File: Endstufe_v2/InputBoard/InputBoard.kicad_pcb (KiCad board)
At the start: 4 copper layers, 57 parts, among them J1 ST-0322D00-071-1A2H, J11 DNP, J2 ST-0322D00-071-1A2H, J3 ST-0322D00-071-1A2H, J4 ST-0322D00-071-1A2H, J5 B4B-XH-2_(LF)(SN), J6 B4B-XH-2_(LF)(SN), J7 B4B-XH-2_(LF)(SN), J8 Conn_01x02_Pin, J9 B4B-XH-2_(LF)(SN), U1 PCM1865DBTR, U2 PCM9211PTR, U4 ZPLR135_T8, U5 ZPLR135_T8, U6 ZPLR135_T8, U7 ZPLR135_T8, Y1 24.576Mhz, Y2 24.576Mhz

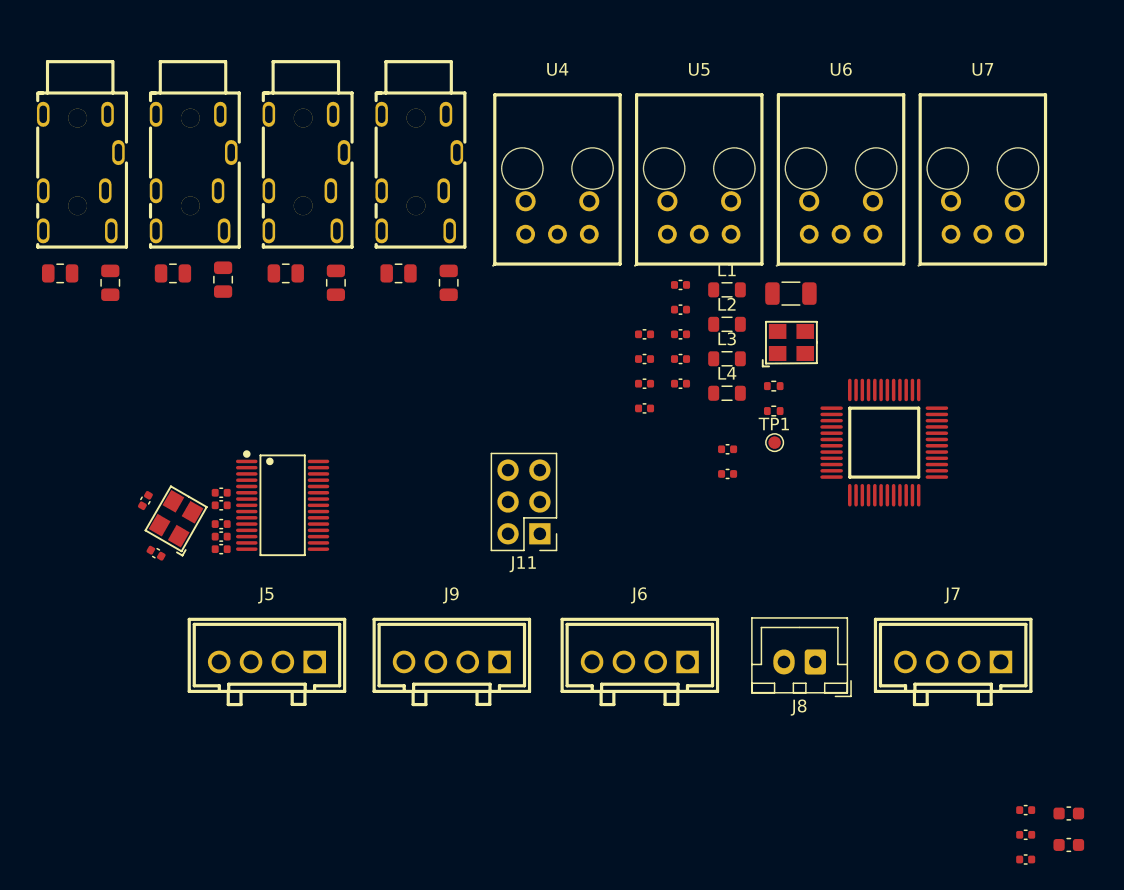
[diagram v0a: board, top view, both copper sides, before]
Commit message: Continue working on input board and use ADAU1467 instaed of ADAU1463
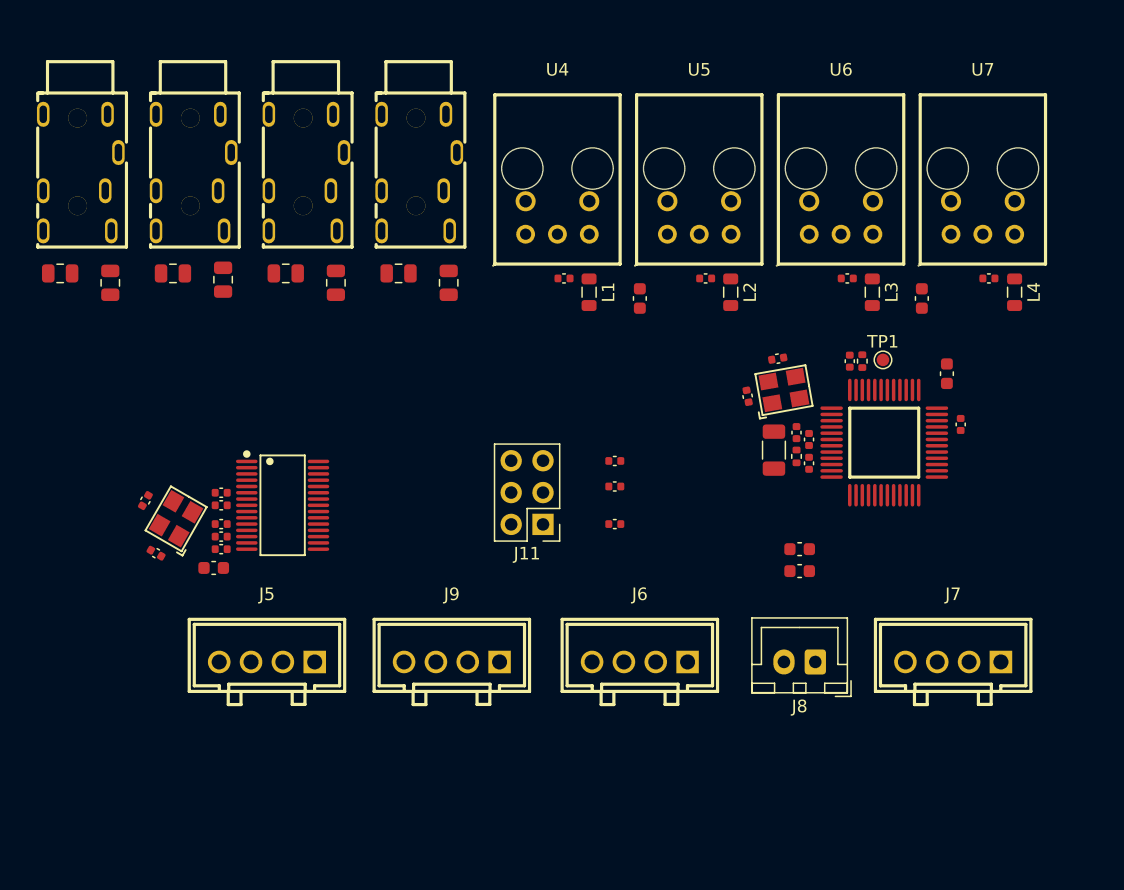
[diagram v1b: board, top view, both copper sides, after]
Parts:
- added C30: 22uF, Endstufe:C_0603_1608Metric, F.Cu at (119.0, 88.0)
- added C31: 22uF, Endstufe:C_0603_1608Metric, F.Cu at (141.5, 88.0)
- added C32: 22uF, Endstufe:C_0603_1608Metric, F.Cu at (85.0, 109.5)
- added C33: 22uF, Endstufe:C_0603_1608Metric, F.Cu at (143.5, 94.0)
- moved R2 43.0 mm to (117.0, 101.0)
- moved R3 43.0 mm to (117.0, 103.0)
- moved R5 42.3 mm to (117.0, 106.0)
- moved C29 30.6 mm to (131.8, 109.8)
- moved C28 30.1 mm to (131.8, 108.0)
- moved C15 25.8 mm to (144.6, 98.0), turned to 90 degrees
- moved C18 24.6 mm to (146.8, 86.4)
- moved L4 24.3 mm to (148.9, 87.5), turned to -90 degrees
- moved C14 16.5 mm to (135.8, 93.0), turned to -90 degrees
- moved C24 15.7 mm to (135.6, 86.4)
- moved C20 14.6 mm to (132.5, 99.2), turned to 90 degrees
- moved C17 13.8 mm to (132.5, 101.2), turned to -90 degrees
- moved L3 12.8 mm to (137.6, 87.5), turned to -90 degrees
- moved C16 12.7 mm to (131.5, 98.7), turned to -90 degrees
- moved C21 12.6 mm to (129.7, 100.1), turned to -90 degrees
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
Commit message: Continue layouting
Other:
- board outline added: 85 x 50 mm
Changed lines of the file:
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@@
 		(tags "capacitor")
 		(property "Reference" "C29"
-			(at 0 -1.43 360)
+			(at 0 -1.43 0)
 			(layer "F.SilkS")
 			(hide yes)
@@
 		)
 		(property "Value" "22uF"
-			(at 0 1.43 360)
+			(at 0 1.43 0)
 			(layer "F.Fab")
 			(effects
@@
 		)
 		(property "Footprint" "Endstufe:C_0603_1608Metric"
-			(at 0 0 360)
+			(at 0 0 0)
 			(layer "F.Fab")
 			(hide yes)
@@
 		)
 		(property "Datasheet" ""
-			(at 0 0 360)
+			(at 0 0 0)
 			(layer "F.Fab")
 			(hide yes)
@@
 		)
 		(property "Description" ""
-			(at 0 0 360)
+			(at 0 0 0)
 			(layer "F.Fab")
 			(hide yes)
@@
 		)
 		(property "LCSC Part #" "C59461"
-			(at 0 0 360)
+			(at 0 0 0)
 			(layer "F.Fab")
 			(hide yes)
@@
 		)
 		(fp_text user "${REFERENCE}"
-			(at 0 0 360)
+			(at 0 0 0)
 			(layer "F.Fab")
 			(effects
@@
 			(end -5 3.694996)
 			(stroke
-				(width 0.254001)
+				(width 0.254)
 				(type solid)
 			)
@@
 			(end 5 -9.805029)
 			(stroke
-				(width 0.254001)
+				(width 0.254)
 				(type solid)
 			)
@@
 			(end 5 3.694996)
 			(stroke
-				(width 0.254001)
+				(width 0.254)
 				(type solid)
 			)
@@
 			(end 5 3.694996)
 			(stroke
-				(width 0.254001)
+				(width 0.254)
 				(type solid)
 			)
@@
 		(tags "capacitor")
 		(property "Reference" "C32"
-			(at 0 -1.43 360)
+			(at 0 -1.43 0)
 			(layer "F.SilkS")
 			(hide yes)
@@
 		)
 		(property "Value" "22uF"
-			(at 0 1.43 360)
+			(at 0 1.43 0)
 			(layer "F.Fab")
 			(effects
@@
 		)
 		(property "Footprint" "Endstufe:C_0603_1608Metric"
-			(at 0 0 360)
+			(at 0 0 0)
 			(layer "F.Fab")
 			(hide yes)
@@
 		)
 		(property "Datasheet" ""
-			(at 0 0 360)
+			(at 0 0 0)
 			(layer "F.Fab")
 			(hide yes)
@@
 		)
 		(property "Description" ""
-			(at 0 0 360)
+			(at 0 0 0)
 			(layer "F.Fab")
 			(hide yes)
@@
 		)
 		(property "LCSC Part #" "C59461"
-			(at 0 0 360)
+			(at 0 0 0)
 			(layer "F.Fab")
 			(hide yes)
@@
 		)
 		(fp_text user "${REFERENCE}"
-			(at 0 0 360)
+			(at 0 0 0)
 			(layer "F.Fab")
 			(effects
@@
 		(tags "capacitor")
 		(property "Reference" "C28"
-			(at 0 -1.43 360)
+			(at 0 -1.43 0)
 			(layer "F.SilkS")
 			(hide yes)
@@
 		)
 		(property "Value" "22uF"
-			(at 0 1.43 360)
+			(at 0 1.43 0)
 			(layer "F.Fab")
 			(effects
@@
 		)
 		(property "Footprint" "Endstufe:C_0603_1608Metric"
-			(at 0 0 360)
+			(at 0 0 0)
 			(layer "F.Fab")
 			(hide yes)
@@
 		)
 		(property "Datasheet" ""
-			(at 0 0 360)
+			(at 0 0 0)
 			(layer "F.Fab")
 			(hide yes)
@@
 		)
 		(property "Description" ""
-			(at 0 0 360)
+			(at 0 0 0)
 			(layer "F.Fab")
 			(hide yes)
@@
 		)
 		(property "LCSC Part #" "C59461"
-			(at 0 0 360)
+			(at 0 0 0)
 			(layer "F.Fab")
 			(hide yes)
@@
 		)
 		(fp_text user "${REFERENCE}"
-			(at 0 0 360)
+			(at 0 0 0)
 			(layer "F.Fab")
 			(effects
@@
 			(end -5 3.694996)
 			(stroke
-				(width 0.254001)
+				(width 0.254)
 				(type solid)
 			)
@@
 			(end 5 -9.805029)
 			(stroke
-				(width 0.254001)
+				(width 0.254)
 				(type solid)
 			)
@@
 			(end 5 3.694996)
 			(stroke
-				(width 0.254001)
+				(width 0.254)
 				(type solid)
 			)
@@
 			(end 5 3.694996)
 			(stroke
-				(width 0.254001)
+				(width 0.254)
 				(type solid)
 			)
@@
 			(end -5 3.694996)
 			(stroke
-				(width 0.254001)
+				(width 0.254)
 				(type solid)
 			)
@@
 			(end 5 -9.805029)
 			(stroke
-				(width 0.254001)
+				(width 0.254)
 				(type solid)
 			)
@@
 			(end 5 3.694996)
 			(stroke
-				(width 0.254001)
+				(width 0.254)
 				(type solid)
 			)
@@
 			(end 5 3.694996)
 			(stroke
-				(width 0.254001)
+				(width 0.254)
 				(type solid)
 			)
@@
 		(tags "capacitor")
 		(property "Reference" "C18"
-			(at 0 -1.16 360)
+			(at 0 -1.16 0)
 			(layer "F.SilkS")
 			(hide yes)
@@
 		)
 		(property "Value" "100nF"
-			(at 0 1.16 360)
+			(at 0 1.16 0)
 			(layer "F.Fab")
 			(effects
@@
 		)
 		(property "Footprint" "Endstufe:C_0402_1005Metric"
-			(at 0 0 360)
+			(at 0 0 0)
 			(layer "F.Fab")
 			(hide yes)
@@
 		)
 		(property "Datasheet" ""
-			(at 0 0 360)
+			(at 0 0 0)
 			(layer "F.Fab")
 			(hide yes)
@@
 		)
 		(property "Description" ""
-			(at 0 0 360)
+			(at 0 0 0)
 			(layer "F.Fab")
 			(hide yes)
@@
 		)
 		(property "LCSC Part #" "C307331"
-			(at 0 0 360)
+			(at 0 0 0)
 			(layer "F.Fab")
 			(hide yes)
@@
 		)
 		(fp_text user "${REFERENCE}"
-			(at 0 0 360)
+			(at 0 0 0)
 			(layer "F.Fab")
 			(effects
@@
 		(tags "capacitor")
 		(property "Reference" "R2"
-			(at 0 -1.16 360)
+			(at 0 -1.16 0)
 			(layer "F.SilkS")
 			(hide yes)
@@
 		)
 		(property "Value" "10k"
-			(at 0 1.16 360)
+			(at 0 1.16 0)
 			(layer "F.Fab")
 			(effects
@@
 		)
 		(property "Footprint" "Endstufe:C_0402_1005Metric"
-			(at 0 0 360)
+			(at 0 0 0)
 			(layer "F.Fab")
 			(hide yes)
@@
 		)
 		(property "Datasheet" ""
-			(at 0 0 360)
+			(at 0 0 0)
 			(layer "F.Fab")
 			(hide yes)
@@
 		)
 		(property "Description" ""
-			(at 0 0 360)
+			(at 0 0 0)
 			(layer "F.Fab")
 			(hide yes)
@@
 		)
 		(property "LCSC Part #" "C25744"
-			(at 0 0 360)
+			(at 0 0 0)
 			(layer "F.Fab")
 			(hide yes)
@@
 		)
 		(fp_text user "${REFERENCE}"
-			(at 0 0 360)
+			(at 0 0 0)
 			(layer "F.Fab")
 			(effects
@@
 			(end -5 3.694996)
 			(stroke
-				(width 0.254001)
+				(width 0.254)
 				(type solid)
 			)
@@
 			(end 5 -9.805029)
 			(stroke
-				(width 0.254001)
+				(width 0.254)
 				(type solid)
 			)
@@
 			(end 5 3.694996)
 			(stroke
-				(width 0.254001)
+				(width 0.254)
 				(type solid)
 			)
@@
 			(end 5 3.694996)
 			(stroke
-				(width 0.254001)
+				(width 0.254)
 				(type solid)
 			)
@@
 		)
 	)
+	(gr_line
+		(start 155 70)
+		(end 155 120)
+		(stroke
+			(width 0.1)
+			(type default)
+		)
+		(layer "Edge.Cuts")
+	)
+	(gr_line
+		(start 70 70)
+		(end 155 70)
+		(stroke
+			(width 0.1)
+			(type default)
+		)
+		(layer "Edge.Cuts")
+	)
+	(gr_line
+		(start 70 120)
+		(end 70 70)
+		(stroke
+			(width 0.1)
+			(type default)
+		)
+		(layer "Edge.Cuts")
+	)
+	(gr_line
+		(start 155 120)
+		(end 70 120)
+		(stroke
+			(width 0.1)
+			(type default)
+		)
+		(layer "Edge.Cuts")
+	)
 )

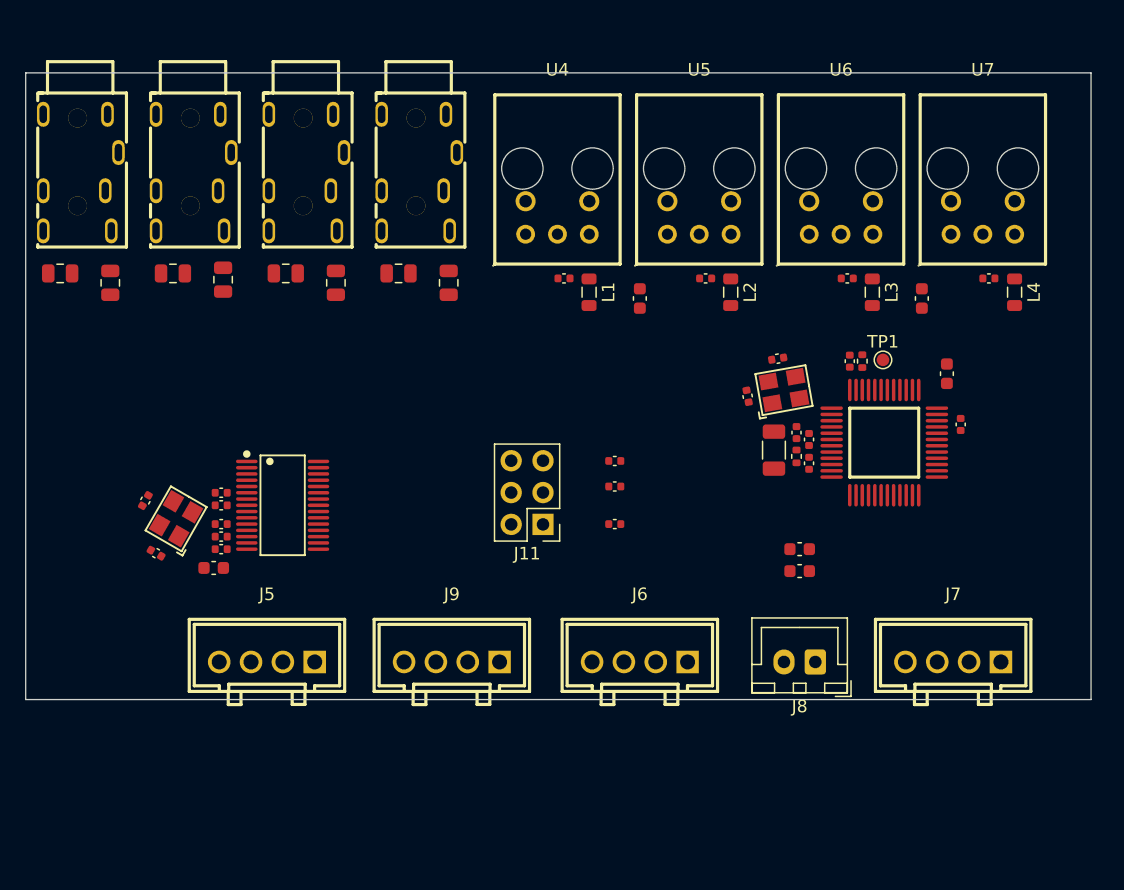
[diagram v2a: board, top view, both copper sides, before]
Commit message: Make mounting holes and continue layouting
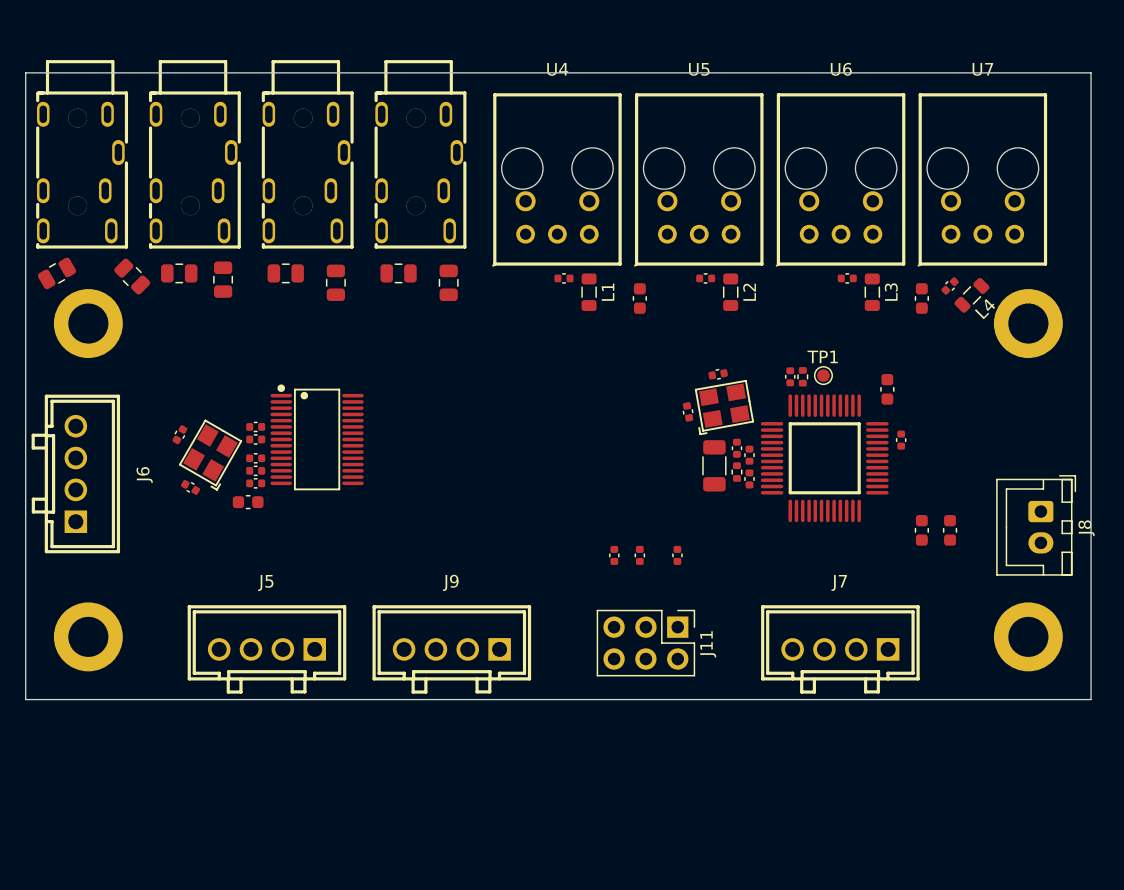
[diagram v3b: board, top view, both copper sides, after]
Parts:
- added H1: MountingHole_Pad, Endstufe:MountingHole_3.2mm_M3_ISO14580_Pad, F.Cu at (75.0, 90.0)
- added H2: MountingHole_Pad, Endstufe:MountingHole_3.2mm_M3_ISO14580_Pad, F.Cu at (150.0, 90.0)
- added H3: MountingHole_Pad, Endstufe:MountingHole_3.2mm_M3_ISO14580_Pad, F.Cu at (75.0, 115.0)
- added H4: MountingHole_Pad, Endstufe:MountingHole_3.2mm_M3_ISO14580_Pad, F.Cu at (150.0, 115.0)
- moved J6 47.4 mm to (74.0, 102.0), turned to -90 degrees
- moved J8 21.6 mm to (151.0, 105.0), turned to -90 degrees
- moved J11 13.5 mm to (122.0, 114.2), turned to -90 degrees
- moved C29 12.4 mm to (143.8, 106.5), turned to 90 degrees
- moved C28 9.86 mm to (141.5, 106.5), turned to 90 degrees
- moved J7 9.06 mm to (135.0, 116.0)
- moved R2 7.54 mm to (117.0, 108.5), turned to 90 degrees
- moved C10 5.93 mm to (88.3, 100.8)
- moved C11 5.93 mm to (88.3, 98.2)
- moved C32 5.93 mm to (87.8, 104.2)
- moved C5 5.93 mm to (82.3, 98.9)
- moved C6 5.93 mm to (83.2, 103.1)
- moved C7 5.93 mm to (88.3, 99.2)
- moved C8 5.93 mm to (88.3, 101.8)
- moved C9 5.93 mm to (88.3, 102.8)
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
